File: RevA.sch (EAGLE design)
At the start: 57 parts, among them IC1 MAX31855, IC10 DS3231/SO, IC3 MAX31855, IC4 MAX31855, IC5 MAX31855, IC9 ATMEGA32U4-AU, J1 1X2-3.5MM, J2 1X2-3.5MM, J3 1X2-3.5MM, J4 1X2-3.5MM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

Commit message: Changes after review
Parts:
- added C10, C11, C12, C20: 1uF, microbuilder:CAP_CERAMIC0603_NO
- added TP1: TPPAD1-13, testpad:TPPAD1-13
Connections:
- removed net 11: IC9.PB7(OC0A/OC1C/RTS)
- removed net 2: IC9.PD1(INT1/SDA)
- removed net 3: IC9.PD0(INT0/OC0B/SCL)
- removed net 3.3V: C19.2, IC10.VCC, R18.1, R19.1
- net +3V3: now also C10.1, C11.1, C12.1, C19.2, C20.1, IC10.VCC, R18.1, R19.1
- net GND: now also C10.2, C11.2, C12.2, C20.2
- net SCL: now also IC9.PD0(INT0/OC0B/SCL)
- net SDA: now also IC9.PD1(INT1/SDA)
- net SD_CS: now also IC9.PB7(OC0A/OC1C/RTS), TP1.TP; no longer IC9.PD4(ICP1/ADC8)
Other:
- moved on the sheet: C18, IC9, R15, R16, R18, R19, X3, Y1

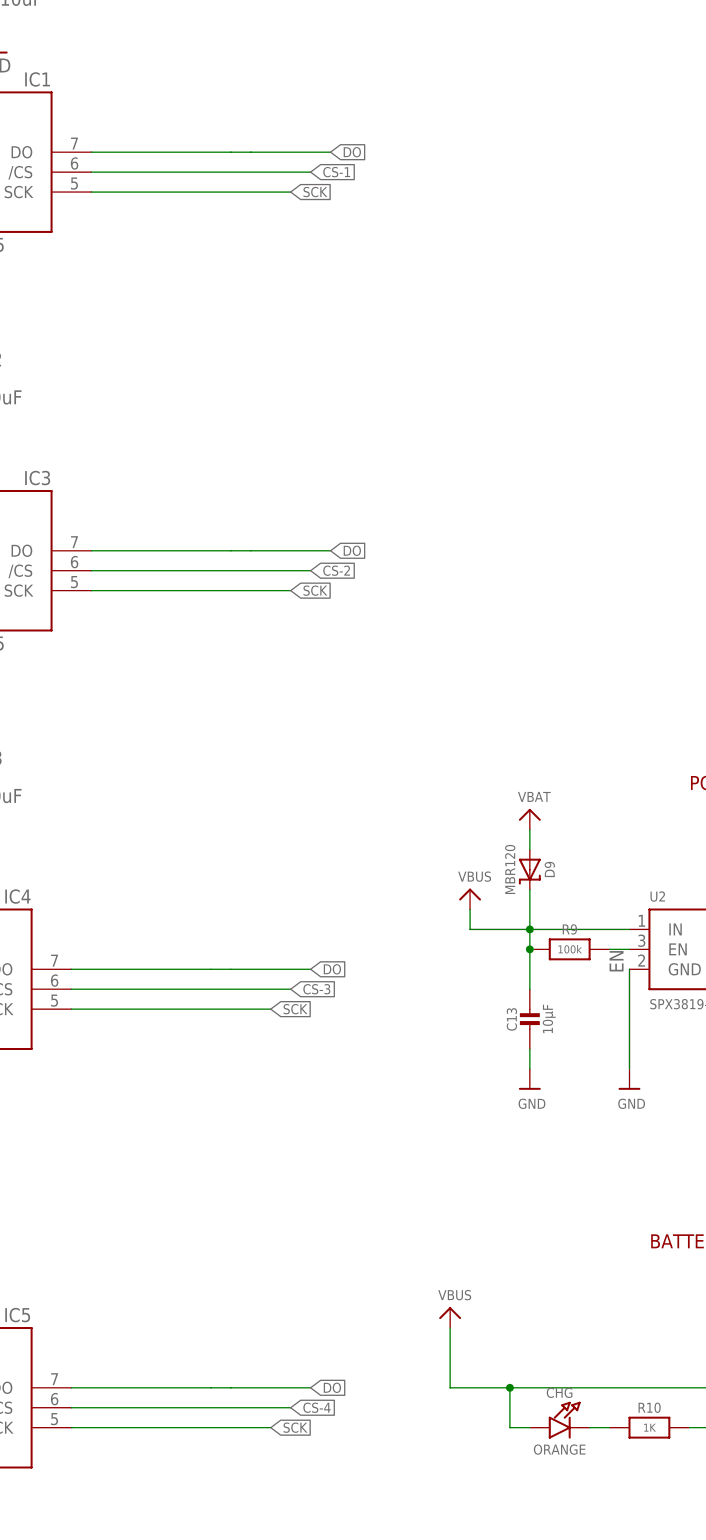
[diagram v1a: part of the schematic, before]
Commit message: Added new layout scheme
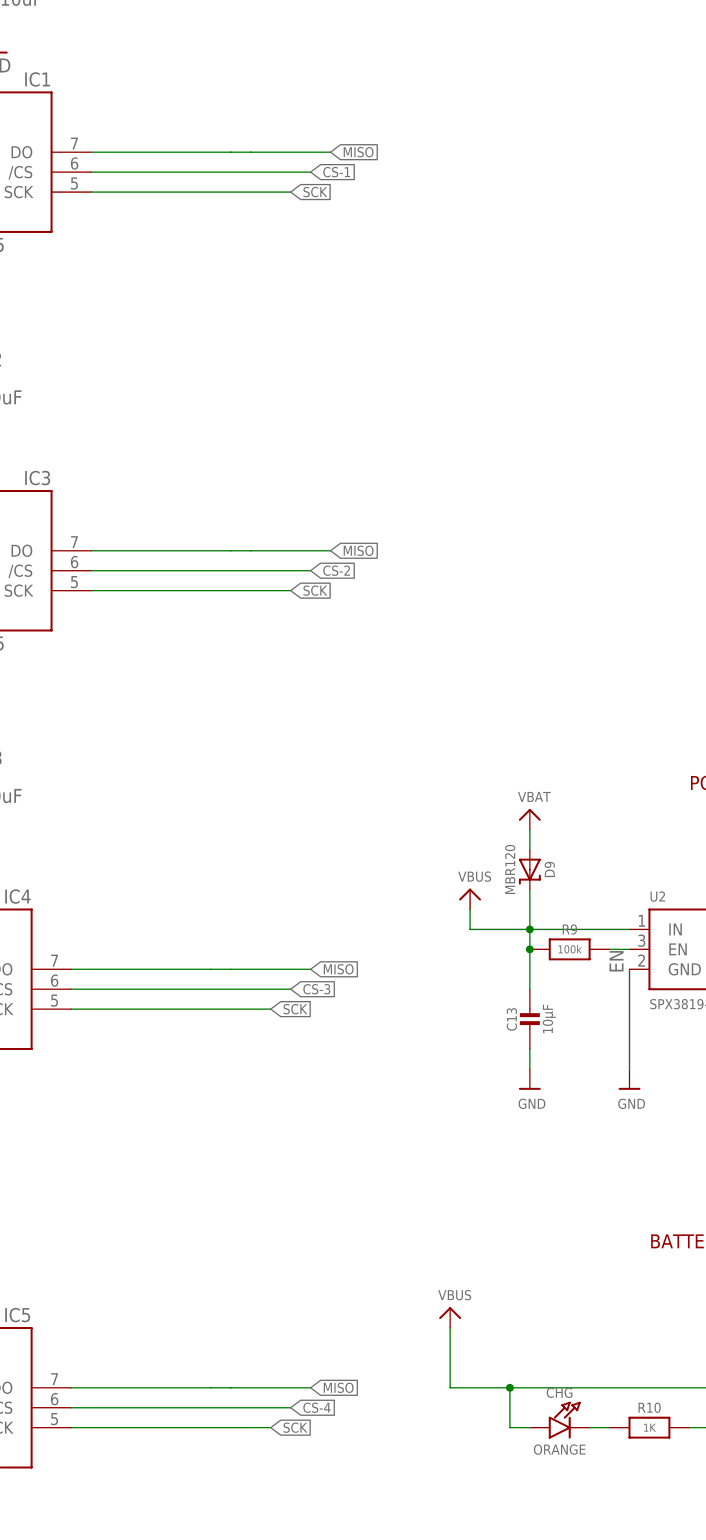
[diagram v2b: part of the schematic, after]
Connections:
- removed net DO: IC1.DO, IC3.DO, IC4.DO, IC5.DO
- net MISO: now also IC1.DO, IC3.DO, IC4.DO, IC5.DO
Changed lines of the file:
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@@
 <?xml version="1.0" encoding="utf-8"?>
 <!DOCTYPE eagle SYSTEM "eagle.dtd">
-<eagle version="9.1.0">
+<eagle version="9.1.2">
 <drawing>
 <settings>
@@
 </segment>
 </net>
-<net name="DO" class="0">
-<segment>
-<wire x1="93.98" y1="182.88" x2="96.52" y2="182.88" width="0.1524" layer="91"/>
-<wire x1="96.52" y1="182.88" x2="106.68" y2="182.88" width="0.1524" layer="91"/>
-<pinref part="IC1" gate="G$1" pin="DO"/>
-<wire x1="76.2" y1="182.88" x2="93.98" y2="182.88" width="0.1524" layer="91"/>
-<label x="106.68" y="182.88" size="1.27" layer="95" xref="yes"/>
-</segment>
-<segment>
-<wire x1="93.98" y1="132.08" x2="96.52" y2="132.08" width="0.1524" layer="91"/>
-<wire x1="96.52" y1="132.08" x2="106.68" y2="132.08" width="0.1524" layer="91"/>
-<pinref part="IC3" gate="G$1" pin="DO"/>
-<wire x1="76.2" y1="132.08" x2="93.98" y2="132.08" width="0.1524" layer="91"/>
-<label x="106.68" y="132.08" size="1.27" layer="95" xref="yes"/>
-</segment>
-<segment>
-<wire x1="91.44" y1="78.74" x2="93.98" y2="78.74" width="0.1524" layer="91"/>
-<wire x1="93.98" y1="78.74" x2="104.14" y2="78.74" width="0.1524" layer="91"/>
-<pinref part="IC4" gate="G$1" pin="DO"/>
-<wire x1="73.66" y1="78.74" x2="91.44" y2="78.74" width="0.1524" layer="91"/>
-<label x="104.14" y="78.74" size="1.27" layer="95" xref="yes"/>
-</segment>
-<segment>
-<wire x1="91.44" y1="25.4" x2="93.98" y2="25.4" width="0.1524" layer="91"/>
-<wire x1="93.98" y1="25.4" x2="104.14" y2="25.4" width="0.1524" layer="91"/>
-<pinref part="IC5" gate="G$1" pin="DO"/>
-<wire x1="73.66" y1="25.4" x2="91.44" y2="25.4" width="0.1524" layer="91"/>
-<label x="104.14" y="25.4" size="1.27" layer="95" xref="yes"/>
-</segment>
-</net>
 <net name="CS-1" class="0">
 <segment>
@@
 <label x="223.52" y="144.78" size="1.27" layer="95" rot="R180" xref="yes"/>
 </segment>
-</net>
+<segment>
+<wire x1="93.98" y1="182.88" x2="96.52" y2="182.88" width="0.1524" layer="91"/>
+<wire x1="96.52" y1="182.88" x2="106.68" y2="182.88" width="0.1524" layer="91"/>
+<pinref part="IC1" gate="G$1" pin="DO"/>
+<wire x1="76.2" y1="182.88" x2="93.98" y2="182.88" width="0.1524" layer="91"/>
+<label x="106.68" y="182.88" size="1.27" layer="95" xref="yes"/>
+</segment>
+<segment>
+<wire x1="93.98" y1="132.08" x2="96.52" y2="132.08" width="0.1524" layer="91"/>
+<wire x1="96.52" y1="132.08" x2="106.68" y2="132.08" width="0.1524" layer="91"/>
+<pinref part="IC3" gate="G$1" pin="DO"/>
+<wire x1="76.2" y1="132.08" x2="93.98" y2="132.08" width="0.1524" layer="91"/>
+<label x="106.68" y="132.08" size="1.27" layer="95" xref="yes"/>
+</segment>
+<segment>
+<wire x1="91.44" y1="78.74" x2="93.98" y2="78.74" width="0.1524" layer="91"/>
+<wire x1="93.98" y1="78.74" x2="104.14" y2="78.74" width="0.1524" layer="91"/>
+<pinref part="IC4" gate="G$1" pin="DO"/>
+<wire x1="73.66" y1="78.74" x2="91.44" y2="78.74" width="0.1524" layer="91"/>
+<label x="104.14" y="78.74" size="1.27" layer="95" xref="yes"/>
+</segment>
+<segment>
+<wire x1="91.44" y1="25.4" x2="93.98" y2="25.4" width="0.1524" layer="91"/>
+<wire x1="93.98" y1="25.4" x2="104.14" y2="25.4" width="0.1524" layer="91"/>
+<pinref part="IC5" gate="G$1" pin="DO"/>
+<wire x1="73.66" y1="25.4" x2="91.44" y2="25.4" width="0.1524" layer="91"/>
+<label x="104.14" y="25.4" size="1.27" layer="95" xref="yes"/>
+</segment>
+</net>

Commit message: Finalized layout and added libraries
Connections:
- removed net 0: IC9.PD2(INT2/RXD1)
- removed net 1: IC9.PD3(INT3/TXD1)
- net CS-1: now also IC9.PD2(INT2/RXD1)
- net CS-2: now also IC9.PD3(INT3/TXD1)
- net CS-3: now also IC9.PD5(XCK/CTS)
- net CS-4: now also IC9.PD4(ICP1/ADC8)
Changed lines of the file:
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@@
 <grid distance="0.1" unitdist="inch" unit="inch" style="lines" multiple="1" display="no" altdistance="0.01" altunitdist="inch" altunit="inch"/>
 <layers>
-<layer number="1" name="Top" color="4" fill="1" visible="yes" active="no"/>
-<layer number="2" name="Route2" color="16" fill="1" visible="yes" active="no"/>
-<layer number="3" name="Route3" color="17" fill="1" visible="yes" active="no"/>
-<layer number="4" name="Route4" color="18" fill="1" visible="yes" active="no"/>
-<layer number="5" name="Route5" color="19" fill="1" visible="yes" active="no"/>
-<layer number="6" name="Route6" color="25" fill="1" visible="yes" active="no"/>
-<layer number="7" name="Route7" color="26" fill="1" visible="yes" active="no"/>
-<layer number="8" name="Route8" color="27" fill="1" visible="yes" active="no"/>
-<layer number="9" name="Route9" color="28" fill="1" visible="yes" active="no"/>
-<layer number="10" name="Route10" color="29" fill="1" visible="yes" active="no"/>
-<layer number="11" name="Route11" color="30" fill="1" visible="yes" active="no"/>
-<layer number="12" name="Route12" color="20" fill="1" visible="yes" active="no"/>
-<layer number="13" name="Route13" color="21" fill="1" visible="yes" active="no"/>
-<layer number="14" name="Route14" color="22" fill="1" visible="yes" active="no"/>
-<layer number="15" name="Route15" color="23" fill="1" visible="yes" active="no"/>
-<layer number="16" name="Bottom" color="1" fill="1" visible="yes" active="no"/>
-<layer number="17" name="Pads" color="2" fill="1" visible="yes" active="no"/>
-<layer number="18" name="Vias" color="2" fill="1" visible="yes" active="no"/>
-<layer number="19" name="Unrouted" color="6" fill="1" visible="yes" active="no"/>
-<layer number="20" name="Dimension" color="24" fill="1" visible="yes" active="no"/>
-<layer number="21" name="tPlace" color="7" fill="1" visible="yes" active="no"/>
-<layer number="22" name="bPlace" color="7" fill="1" visible="yes" active="no"/>
-<layer number="23" name="tOrigins" color="15" fill="1" visible="yes" active="no"/>
-<layer number="24" name="bOrigins" color="15" fill="1" visible="yes" active="no"/>
-<layer number="25" name="tNames" color="7" fill="1" visible="yes" active="no"/>
-<layer number="26" name="bNames" color="7" fill="1" visible="yes" active="no"/>
-<layer number="27" name="tValues" color="7" fill="1" visible="yes" active="no"/>
-<layer number="28" name="bValues" color="7" fill="1" visible="yes" active="no"/>
+<layer number="1" name="Top" color="4" fill="1" visible="no" active="no"/>
+<layer number="2" name="Route2" color="16" fill="1" visible="no" active="no"/>
+<layer number="3" name="Route3" color="17" fill="1" visible="no" active="no"/>
+<layer number="4" name="Route4" color="18" fill="1" visible="no" active="no"/>
+<layer number="5" name="Route5" color="19" fill="1" visible="no" active="no"/>
+<layer number="6" name="Route6" color="25" fill="1" visible="no" active="no"/>
+<layer number="7" name="Route7" color="26" fill="1" visible="no" active="no"/>
+<layer number="8" name="Route8" color="27" fill="1" visible="no" active="no"/>
+<layer number="9" name="Route9" color="28" fill="1" visible="no" active="no"/>
+<layer number="10" name="Route10" color="29" fill="1" visible="no" active="no"/>
+<layer number="11" name="Route11" color="30" fill="1" visible="no" active="no"/>
+<layer number="12" name="Route12" color="20" fill="1" visible="no" active="no"/>
+<layer number="13" name="Route13" color="21" fill="1" visible="no" active="no"/>
+<layer number="14" name="Route14" color="22" fill="1" visible="no" active="no"/>
+<layer number="15" name="Route15" color="23" fill="1" visible="no" active="no"/>
+<layer number="16" name="Bottom" color="1" fill="1" visible="no" active="no"/>
+<layer number="17" name="Pads" color="2" fill="1" visible="no" active="no"/>
+<layer number="18" name="Vias" color="2" fill="1" visible="no" active="no"/>
+<layer number="19" name="Unrouted" color="6" fill="1" visible="no" active="no"/>
+<layer number="20" name="Dimension" color="24" fill="1" visible="no" active="no"/>
+<layer number="21" name="tPlace" color="7" fill="1" visible="no" active="no"/>
+<layer number="22" name="bPlace" color="7" fill="1" visible="no" active="no"/>
+<layer number="23" name="tOrigins" color="15" fill="1" visible="no" active="no"/>
+<layer number="24" name="bOrigins" color="15" fill="1" visible="no" active="no"/>
+<layer number="25" name="tNames" color="7" fill="1" visible="no" active="no"/>
+<layer number="26" name="bNames" color="7" fill="1" visible="no" active="no"/>
+<layer number="27" name="tValues" color="7" fill="1" visible="no" active="no"/>
+<layer number="28" name="bValues" color="7" fill="1" visible="no" active="no"/>
 <layer number="29" name="tStop" color="7" fill="3" visible="no" active="no"/>
 <layer number="30" name="bStop" color="7" fill="6" visible="no" active="no"/>
@@
 <layer number="35" name="tGlue" color="7" fill="4" visible="no" active="no"/>
 <layer number="36" name="bGlue" color="7" fill="5" visible="no" active="no"/>
-<layer number="37" name="tTest" color="7" fill="1" visible="yes" active="no"/>
-<layer number="38" name="bTest" color="7" fill="1" visible="yes" active="no"/>
+<layer number="37" name="tTest" color="7" fill="1" visible="no" active="no"/>
+<layer number="38" name="bTest" color="7" fill="1" visible="no" active="no"/>
 <layer number="39" name="tKeepout" color="4" fill="11" visible="no" active="no"/>
 <layer number="40" name="bKeepout" color="1" fill="11" visible="no" active="no"/>
@@
 <layer number="44" name="Drills" color="7" fill="1" visible="no" active="no"/>
 <layer number="45" name="Holes" color="7" fill="1" visible="no" active="no"/>
-<layer number="46" name="Milling" color="3" fill="1" visible="yes" active="no"/>
-<layer number="47" name="Measures" color="7" fill="1" visible="yes" active="no"/>
-<layer number="48" name="Document" color="7" fill="1" visible="yes" active="no"/>
-<layer number="49" name="Reference" color="7" fill="1" visible="yes" active="no"/>
-<layer number="50" name="dxf" color="7" fill="1" visible="yes" active="no"/>
-<layer number="51" name="tDocu" color="7" fill="1" visible="yes" active="no"/>
-<layer number="52" name="bDocu" color="7" fill="1" visible="yes" active="no"/>
-<layer number="53" name="tGND_GNDA" color="7" fill="9" visible="yes" active="no"/>
-<layer number="54" name="bGND_GNDA" color="1" fill="9" visible="yes" active="no"/>
-<layer number="56" name="wert" color="7" fill="1" visible="yes" active="no"/>
-<layer number="57" name="tCAD" color="7" fill="1" visible="yes" active="no"/>
-<layer number="59" name="tCarbon" color="7" fill="1" visible="yes" active="no"/>
-<layer number="60" name="bCarbon" color="7" fill="1" visible="yes" active="no"/>
+<layer number="46" name="Milling" color="3" fill="1" visible="no" active="no"/>
+<layer number="47" name="Measures" color="7" fill="1" visible="no" active="no"/>
+<layer number="48" name="Document" color="7" fill="1" visible="no" active="no"/>
+<layer number="49" name="Reference" color="7" fill="1" visible="no" active="no"/>
+<layer number="50" name="dxf" color="7" fill="1" visible="no" active="no"/>
+<layer number="51" name="tDocu" color="7" fill="1" visible="no" active="no"/>
+<layer number="52" name="bDocu" color="7" fill="1" visible="no" active="no"/>
+<layer number="53" name="tGND_GNDA" color="7" fill="9" visible="no" active="no"/>
+<layer number="54" name="bGND_GNDA" color="1" fill="9" visible="no" active="no"/>
+<layer number="56" name="wert" color="7" fill="1" visible="no" active="no"/>
+<layer number="57" name="tCAD" color="7" fill="1" visible="no" active="no"/>
+<layer number="59" name="tCarbon" color="7" fill="1" visible="no" active="no"/>
+<layer number="60" name="bCarbon" color="7" fill="1" visible="no" active="no"/>
 <layer number="88" name="SimResults" color="9" fill="1" visible="yes" active="yes"/>
 <layer number="89" name="SimProbes" color="9" fill="1" visible="yes" active="yes"/>
@@
 <label x="104.14" y="180.34" size="1.27" layer="95" xref="yes"/>
 </segment>
+<segment>
+<pinref part="IC9" gate="G$1" pin="PD2(INT2/RXD1)"/>
+<wire x1="457.2" y1="167.64" x2="441.96" y2="167.64" width="0.1524" layer="91"/>
+<label x="444.5" y="167.64" size="1.778" layer="95"/>
+<label x="457.2" y="167.64" size="1.778" layer="95" xref="yes"/>
+</segment>
 </net>
 <net name="+3V3" class="0">
@@
 </segment>
 </net>
-<net name="1" class="0">
-<segment>
-<pinref part="IC9" gate="G$1" pin="PD3(INT3/TXD1)"/>
-<wire x1="441.96" y1="170.18" x2="457.2" y2="170.18" width="0.1524" layer="91"/>
-<label x="444.5" y="170.18" size="1.778" layer="95"/>
-</segment>
-</net>
-<net name="0" class="0">
-<segment>
-<pinref part="IC9" gate="G$1" pin="PD2(INT2/RXD1)"/>
-<wire x1="457.2" y1="167.64" x2="441.96" y2="167.64" width="0.1524" layer="91"/>
-<label x="444.5" y="167.64" size="1.778" layer="95"/>
-</segment>
-</net>
 <net name="13" class="0">
 <segment>
@@
 <label x="104.14" y="129.54" size="1.27" layer="95" xref="yes"/>
 </segment>
+<segment>
+<pinref part="IC9" gate="G$1" pin="PD3(INT3/TXD1)"/>
+<wire x1="441.96" y1="170.18" x2="457.2" y2="170.18" width="0.1524" layer="91"/>
+<label x="444.5" y="170.18" size="1.778" layer="95"/>
+<label x="457.2" y="170.18" size="1.778" layer="95" xref="yes"/>
+</segment>
 </net>
 <net name="CS-3" class="0">
@@
 <label x="101.6" y="76.2" size="1.27" layer="95" xref="yes"/>
 </segment>
+<segment>
+<pinref part="IC9" gate="G$1" pin="PD5(XCK/CTS)"/>
+<wire x1="441.96" y1="175.26" x2="457.2" y2="175.26" width="0.1524" layer="91"/>
+<label x="457.2" y="175.26" size="1.778" layer="95" xref="yes"/>
+</segment>
 </net>
 <net name="CS-4" class="0">
@@
 <label x="101.6" y="22.86" size="1.27" layer="95" xref="yes"/>
 </segment>
-</net>
+<segment>
+<pinref part="IC9" gate="G$1" pin="PD4(ICP1/ADC8)"/>
+<wire x1="441.96" y1="172.72" x2="457.2" y2="172.72" width="0.1524" layer="91"/>
+<label x="457.2" y="172.72" size="1.778" layer="95" xref="yes"/>
+</segment>
+</net>

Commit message: More Revision
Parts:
- removed R9: 100k, microbuilder:RESISTOR_0603_NOOUT
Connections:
- removed net EN: R9.2, U2.EN
- new net COIN: B1.+, IC10.VBAT
- net VBAT: no longer B1.+, IC10.VBAT
- net VBUS: now also U2.EN; no longer R9.1
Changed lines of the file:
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@@
 <?xml version="1.0" encoding="utf-8"?>
 <!DOCTYPE eagle SYSTEM "eagle.dtd">
-<eagle version="9.1.2">
+<eagle version="9.1.0">
 <drawing>
 <settings>
@@
 <part name="U$18" library="microbuilder" deviceset="VBAT" device=""/>
 <part name="U$22" library="microbuilder" deviceset="GND" device=""/>
-<part name="R9" library="microbuilder" deviceset="RESISTOR" device="_0603_NOOUT" value="100k"/>
 <part name="U3" library="microbuilder" deviceset="MCP73831/2" device="" value="MCP73831T-2ACI/OT"/>
 <part name="CHG" library="microbuilder" deviceset="LED" device="0805_NOOUTLINE" value="ORANGE"/>
@@
 <instance part="U$18" gate="G$1" x="190.5" y="86.36"/>
 <instance part="U$22" gate="G$1" x="190.5" y="63.5"/>
-<instance part="R9" gate="G$1" x="137.16" y="81.28"/>
 <instance part="U3" gate="G$1" x="170.18" y="22.86"/>
 <instance part="CHG" gate="G$1" x="137.16" y="20.32"/>
@@
 <pinref part="D9" gate="G$1" pin="C"/>
 <wire x1="124.46" y1="83.82" x2="132.08" y2="83.82" width="0.1524" layer="91"/>
-<pinref part="R9" gate="G$1" pin="1"/>
+<pinref part="U2" gate="G$1" pin="EN"/>
+<wire x1="144.78" y1="81.28" x2="132.08" y2="81.28" width="0.1524" layer="91"/>
 <junction x="132.08" y="81.28"/>
 </segment>
@@
 <pinref part="U$19" gate="G$1" pin="VBAT"/>
 </segment>
-<segment>
-<pinref part="B1" gate="G$1" pin="+"/>
-<wire x1="307.34" y1="30.48" x2="307.34" y2="25.4" width="0.1524" layer="91"/>
-<pinref part="IC10" gate="G$1" pin="VBAT"/>
-<wire x1="294.64" y1="30.48" x2="307.34" y2="30.48" width="0.1524" layer="91"/>
-<wire x1="307.34" y1="30.48" x2="314.96" y2="30.48" width="0.1524" layer="91"/>
-<junction x="307.34" y="30.48"/>
-<label x="314.96" y="30.48" size="1.27" layer="95" xref="yes"/>
-</segment>
-</net>
-<net name="EN" class="0">
-<segment>
-<pinref part="U2" gate="G$1" pin="EN"/>
-<pinref part="R9" gate="G$1" pin="2"/>
-<wire x1="142.24" y1="81.28" x2="144.78" y2="81.28" width="0.1524" layer="91"/>
-<label x="142.24" y="81.28" size="1.778" layer="95" rot="R270"/>
-</segment>
 </net>
 <net name="9" class="0">
@@
 </segment>
 </net>
+<net name="COIN" class="0">
+<segment>
+<pinref part="B1" gate="G$1" pin="+"/>
+<wire x1="307.34" y1="30.48" x2="307.34" y2="25.4" width="0.1524" layer="91"/>
+<pinref part="IC10" gate="G$1" pin="VBAT"/>
+<wire x1="294.64" y1="30.48" x2="307.34" y2="30.48" width="0.1524" layer="91"/>
+</segment>
+</net>

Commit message: Changed Layout
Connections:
- net COIN renamed VCR
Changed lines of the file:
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@@
 <?xml version="1.0" encoding="utf-8"?>
 <!DOCTYPE eagle SYSTEM "eagle.dtd">
-<eagle version="9.1.0">
+<eagle version="9.1.2">
 <drawing>
 <settings>
@@
 </segment>
 </net>
-<net name="COIN" class="0">
+<net name="VCR" class="0">
 <segment>
 <pinref part="B1" gate="G$1" pin="+"/>
